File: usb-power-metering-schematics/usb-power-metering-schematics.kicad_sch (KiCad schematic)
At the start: 7 parts, among them U2 ATmega328P-P, Y1 16MHz

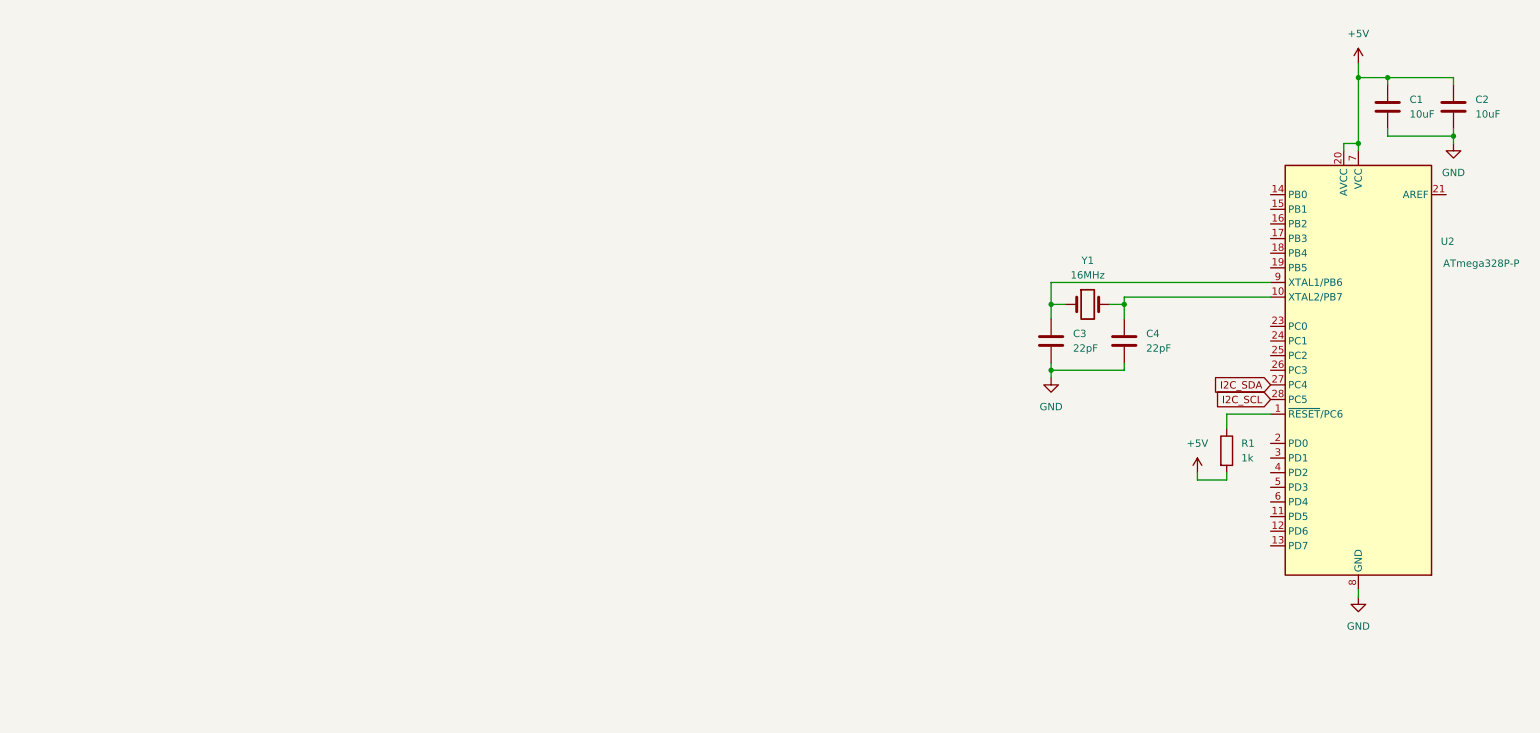
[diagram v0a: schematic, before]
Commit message: add ina219 implementation to schematics
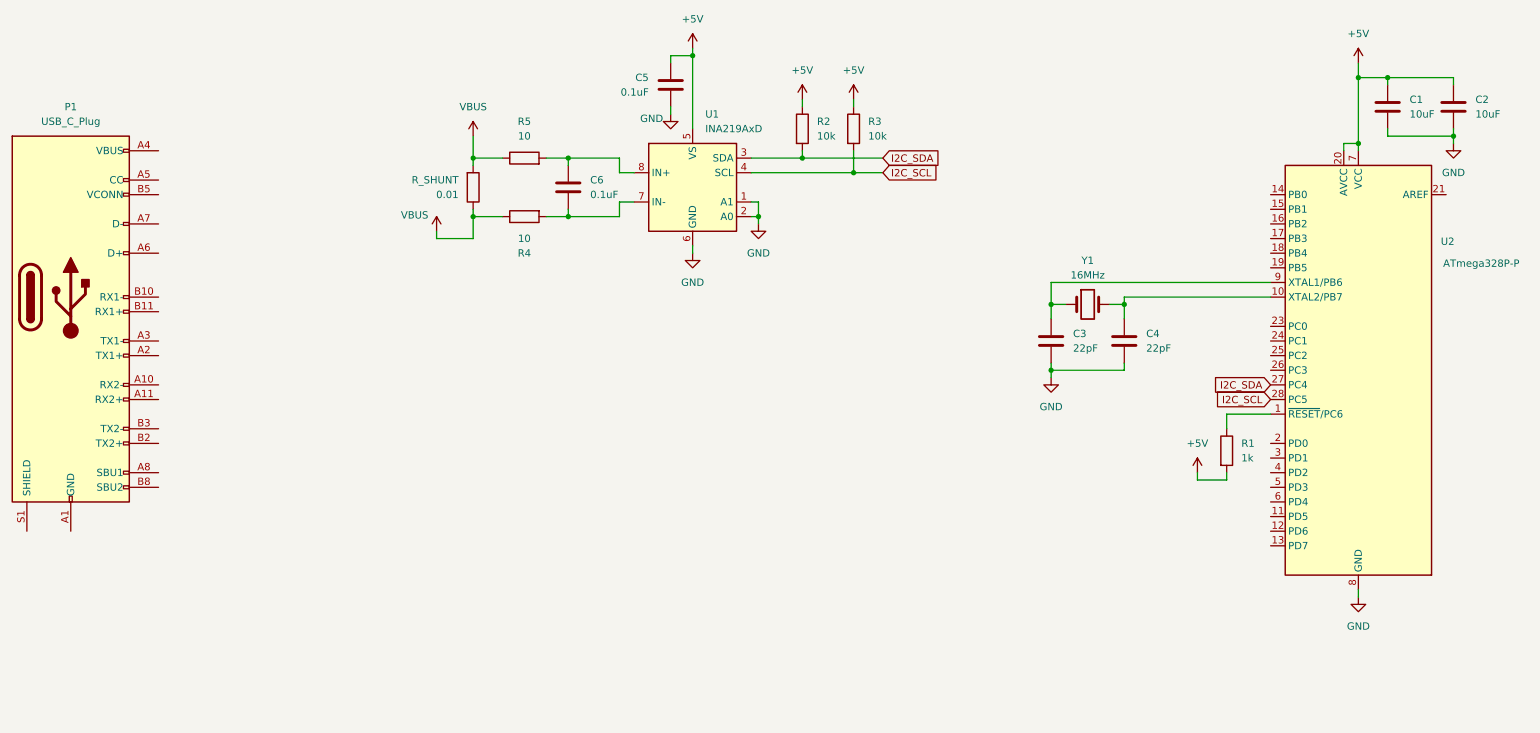
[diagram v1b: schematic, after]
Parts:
- added C5, C6: 0.1uF, symbol Device:C
- added P1: USB_C_Plug, symbol Connector:USB_C_Plug
- added R2, R3: 10k, symbol Device:R
- added R4, R5: 10, symbol Device:R
- added R_SHUNT: 0.01, symbol Device:R
- added U1: INA219AxD, Package_SO:SOIC-8_3.9x4.9mm_P1.27mm, symbol Sensor_Energy:INA219AxD
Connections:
- net +5V: now also C5.1, R2.1, R3.1, U1.5 (VS)
- net GND: now also C5.2, U1.1 (A1), U1.2 (A0), U1.6 (GND)
- net I2C_SCL: now also R3.2, U1.4 (SCL)
- net I2C_SDA: now also R2.2, U1.3 (SDA)
- new net: C6.2, R4.2, U1.7 (IN-)
- new net: C6.1, R5.2, U1.8 (IN+)
- new net: P1.A1 (GND), P1.A12 (GND), P1.B1 (GND), P1.B12 (GND)
- new net: P1.A4 (VBUS), P1.A9 (VBUS), P1.B4 (VBUS), P1.B9 (VBUS)
- new net VBUS: R4.1, R5.1, R_SHUNT.1, R_SHUNT.2

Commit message: add HUSB238 to schematics & fix symbol issue
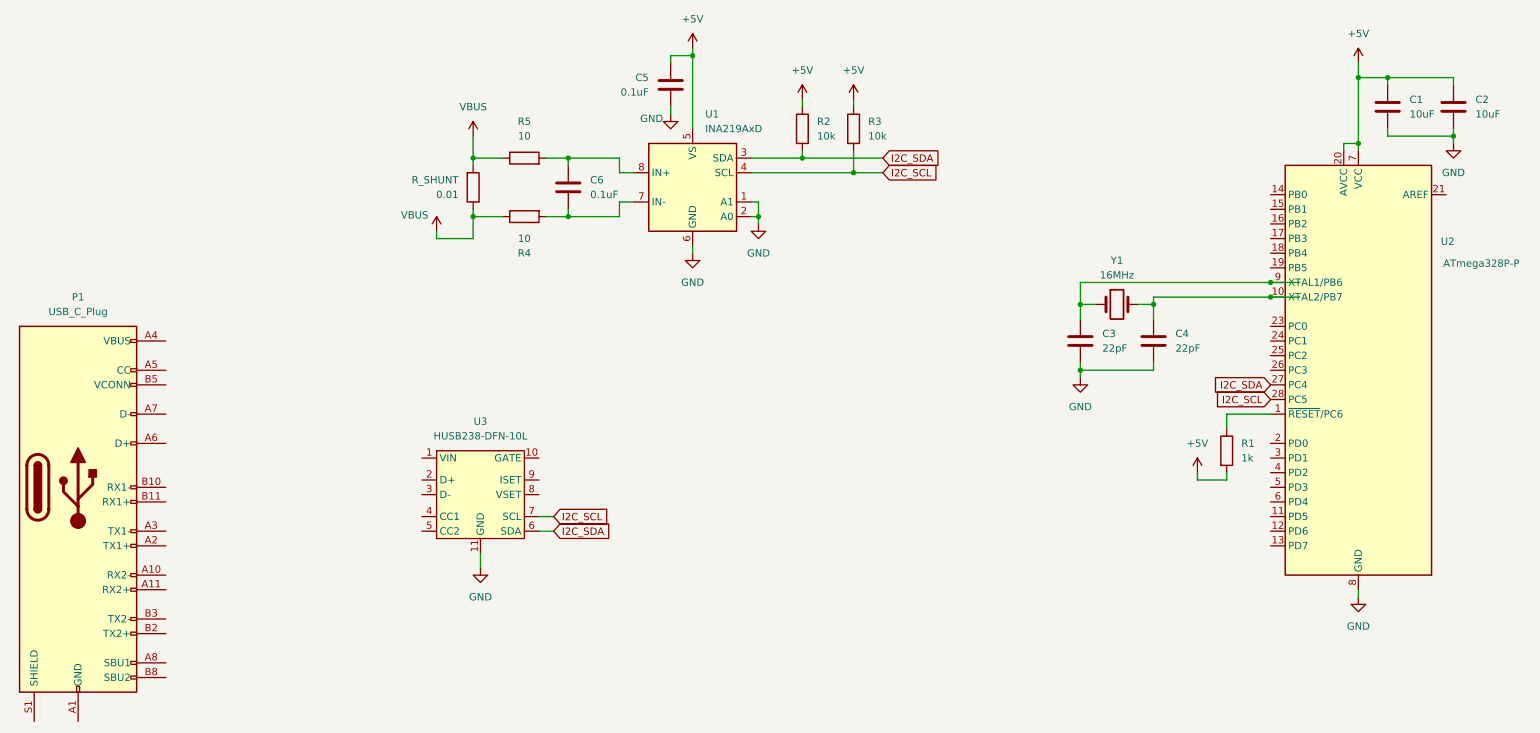
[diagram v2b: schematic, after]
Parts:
- added U3: HUSB238-DFN-10L, symbol HUSB238:HUSB238-DFN-10L
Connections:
- net GND: now also U3.11 (GND)
- net I2C_SCL: now also U3.7 (SCL)
- net I2C_SDA: now also U3.6 (SDA)
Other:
- company: (none) -> ritonun
- title: (none) -> usb-power-metering
- moved on the sheet: C3, C4, P1, Y1
